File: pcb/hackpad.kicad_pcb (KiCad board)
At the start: 2 copper layers, 21.5 x 50 mm, 4 parts, among them SW1 SW_Push, SW2 SW_Push, SW3 SW_Push, U1 MOUDLE-SEEEDUINO-XIAO

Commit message: Update the schematic
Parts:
- added D1: 1N4148, Diode_THT:D_DO-35_SOD27_P7.62mm_Horizontal, F.Cu at (49.0, 84.6)
- added D10: 1N4148, Diode_THT:D_DO-35_SOD27_P7.62mm_Horizontal, F.Cu at (68.0, 122.7)
- added D11: 1N4148, Diode_THT:D_DO-35_SOD27_P7.62mm_Horizontal, F.Cu at (87.1, 122.7)
- added D12: 1N4148, Diode_THT:D_DO-35_SOD27_P7.62mm_Horizontal, F.Cu at (106.2, 122.7)
- added D2: 1N4148, Diode_THT:D_DO-35_SOD27_P7.62mm_Horizontal, F.Cu at (68.0, 84.6)
- added D3: 1N4148, Diode_THT:D_DO-35_SOD27_P7.62mm_Horizontal, F.Cu at (87.1, 84.6)
- added D4: 1N4148, Diode_THT:D_DO-35_SOD27_P7.62mm_Horizontal, F.Cu at (106.2, 84.6)
- added D5: 1N4148, Diode_THT:D_DO-35_SOD27_P7.62mm_Horizontal, F.Cu at (49.0, 103.7)
- added D6: 1N4148, Diode_THT:D_DO-35_SOD27_P7.62mm_Horizontal, F.Cu at (68.0, 103.7)
- added D7: 1N4148, Diode_THT:D_DO-35_SOD27_P7.62mm_Horizontal, F.Cu at (87.1, 103.7)
- added D8: 1N4148, Diode_THT:D_DO-35_SOD27_P7.62mm_Horizontal, F.Cu at (106.2, 103.7)
- added D9: 1N4148, Diode_THT:D_DO-35_SOD27_P7.62mm_Horizontal, F.Cu at (49.0, 122.7)
- added SW10: SW_Push, Button_Switch_Keyboard:SW_Cherry_MX_1.00u_PCB, F.Cu at (79.0, 108.1)
- added SW11: SW_Push, Button_Switch_Keyboard:SW_Cherry_MX_1.00u_PCB, F.Cu at (98.1, 108.1)
- added SW12: SW_Push, Button_Switch_Keyboard:SW_Cherry_MX_1.00u_PCB, F.Cu at (117.2, 108.1)
- added SW13: RotaryEncoder_Switch, Rotary_Encoder:RotaryEncoder_Alps_EC11E-Switch_Vertical_H20mm, F.Cu at (50.2, 47.5)
- added SW4: SW_Push, Button_Switch_Keyboard:SW_Cherry_MX_1.00u_PCB, F.Cu at (117.2, 70.0)
- added SW5: SW_Push, Button_Switch_Keyboard:SW_Cherry_MX_1.00u_PCB, F.Cu at (60.0, 89.0)
- added SW6: SW_Push, Button_Switch_Keyboard:SW_Cherry_MX_1.00u_PCB, F.Cu at (79.0, 89.0)
- added SW7: SW_Push, Button_Switch_Keyboard:SW_Cherry_MX_1.00u_PCB, F.Cu at (98.1, 89.0)
- added SW8: SW_Push, Button_Switch_Keyboard:SW_Cherry_MX_1.00u_PCB, F.Cu at (117.2, 89.0)
- added SW9: SW_Push, Button_Switch_Keyboard:SW_Cherry_MX_1.00u_PCB, F.Cu at (60.0, 108.1)
- added U2: ER_OLEDM0.91_1x-I2C, Display:ER_OLEDM0.91_1x-I2C, F.Cu at (121.0, 46.7)
- moved SW1 39.2 mm to (60.0, 70.0)
- moved SW2 14.9 mm to (79.0, 70.0)
- moved U1 14.0 mm to (75.1, 52.4)
- moved SW3 9.43 mm to (98.1, 70.0)
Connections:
- SW1 pad 1: Net-(U1-PA6_A10_D10_MOSI) -> /Column 0
- SW1 pad 2: GND -> Net-(D1-A)
- SW2 pad 1: Net-(U1-PA5_A9_D9_MISO) -> /Column 1
- SW2 pad 2: GND -> Net-(D2-A)
- SW3 pad 1: Net-(U1-PA7_A8_D8_SCK) -> /Column 2
- SW3 pad 2: GND -> Net-(D3-A)
- U1 pad 1: unconnected-(U1-PA02_A0_D0-Pad1) -> /Column 0
- U1 pad 12: unconnected-(U1-3V3-Pad12) -> Net-(U1-3V3)
- U1 pad 2: unconnected-(U1-PA4_A1_D1-Pad2) -> /Column 1
- U1 pad 3: unconnected-(U1-PA10_A2_D2-Pad3) -> /Column 2
- U1 pad 4: unconnected-(U1-PA11_A3_D3-Pad4) -> /Column 3
- U1 pad 5: unconnected-(U1-PA8_A4_D4_SDA-Pad5) -> OLED SDA
- U1 pad 6: unconnected-(U1-PA9_A5_D5_SCL-Pad6) -> OLED SCL
- U1 pad 7: unconnected-(U1-PB08_A6_D6_TX-Pad7) -> Net-(D1-K)
- U1 pad 8: unconnected-(U1-PB09_A7_D7_RX-Pad8) -> /Row 1
- U1 pad 9: Net-(U1-PA7_A8_D8_SCK) -> /Row 2
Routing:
- net GND: track 30.2 -> 0.00 mm
- net Net-(U1-PA7_A8_D8_SCK): track 26.2 -> 0.00 mm
- net Net-(U1-PA6_A10_D10_MOSI): track 17.2 -> 0.00 mm
- net Net-(U1-PA5_A9_D9_MISO): track 14.7 -> 0.00 mm
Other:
- board size 21.5 x 50 mm -> 100 x 100 mm

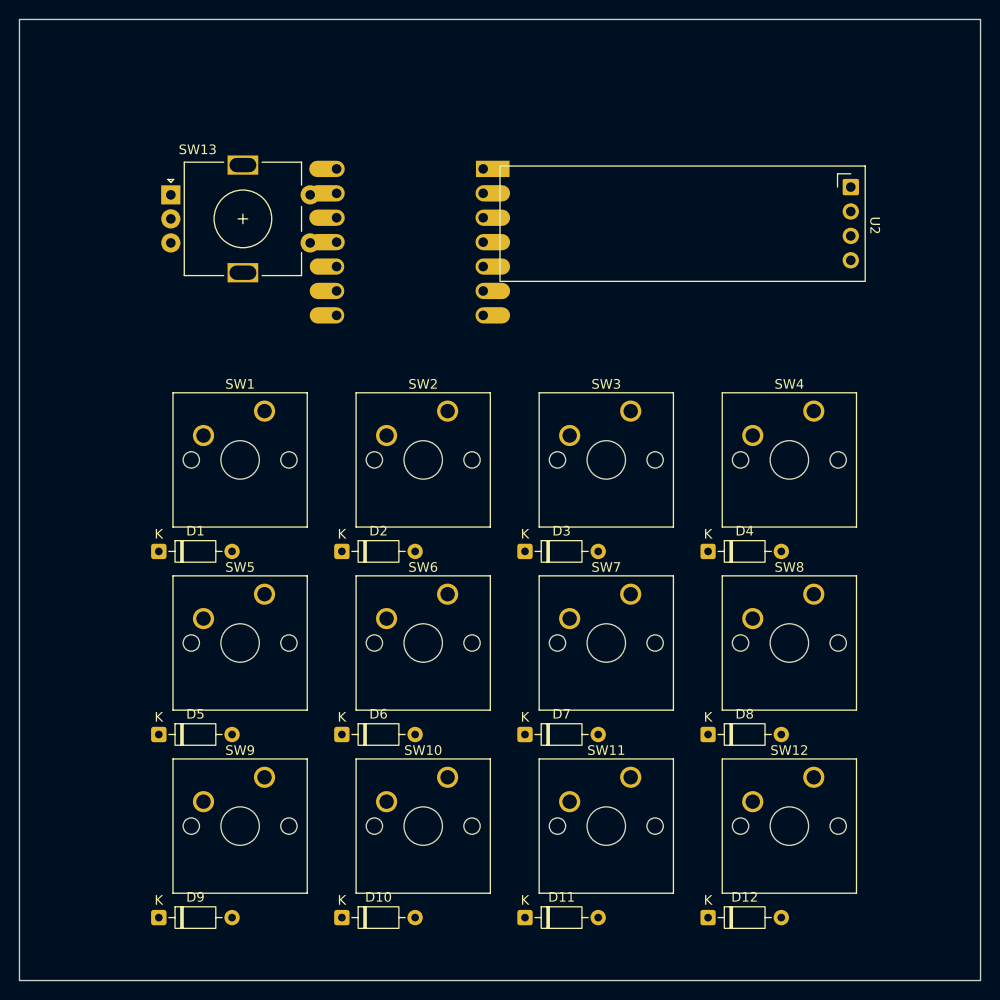
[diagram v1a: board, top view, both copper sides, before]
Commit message: Re-route PCB and update the case
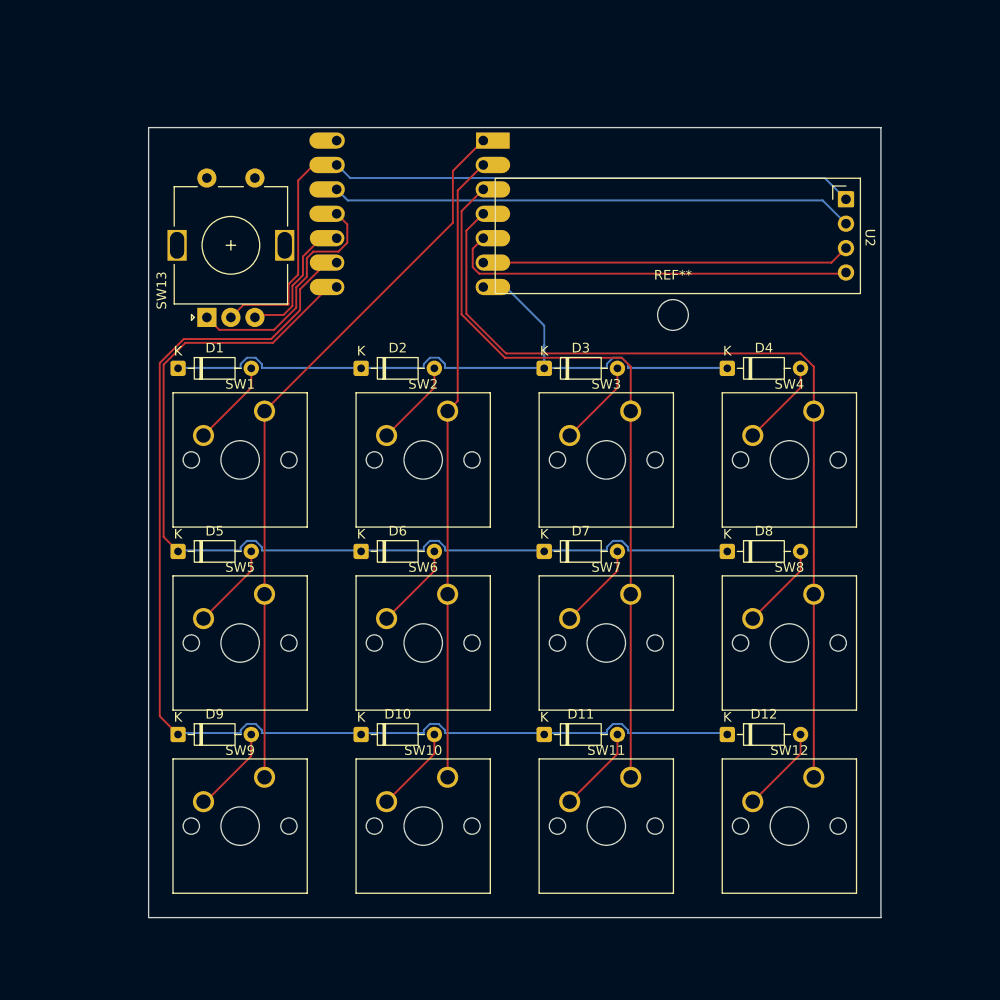
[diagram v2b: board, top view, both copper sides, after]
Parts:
- added REF**: MountingHole_3.2mm_M3, MountingHole:MountingHole_3.2mm_M3, F.Cu at (102.5, 60.0)
- moved D5 19.2 mm to (51.0, 84.6)
- moved D6 19.2 mm to (70.0, 84.6)
- moved D7 19.2 mm to (89.1, 84.6)
- moved D8 19.2 mm to (108.2, 84.6)
- moved D1 19.2 mm to (51.0, 65.5)
- moved D10 19.2 mm to (70.0, 103.7)
- moved D11 19.2 mm to (89.1, 103.7)
- moved D12 19.2 mm to (108.2, 103.7)
- moved D2 19.2 mm to (70.0, 65.5)
- moved D3 19.2 mm to (89.1, 65.5)
- moved D4 19.2 mm to (108.2, 65.5)
- moved D9 19.2 mm to (51.0, 103.7)
- moved SW13 13.3 mm to (54.0, 60.2), turned to 90 degrees
- moved U1 2.95 mm to (75.1, 49.5)
- moved U2 1.36 mm to (120.5, 48.0)
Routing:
- net /Row 2: track 0.00 -> 125.4 mm
- net /Row 1: track 0.00 -> 103.3 mm
- net /Column 3: track 0.00 -> 92.3 mm
- net GND: track 0.00 -> 81.5 mm
- net Net-(D1-K): track 0.00 -> 78.5 mm
- net /Column 2: track 0.00 -> 76.5 mm
- net /Column 0: track 0.00 -> 75.7 mm
- net /Column 1: track 0.00 -> 65.2 mm
- net Net-(U1-3V3): track 0.00 -> 54.5 mm
- net OLED SDA: track 0.00 -> 42.6 mm
- net OLED SCL: track 0.00 -> 38.4 mm
- net Net-(U1-PA6_A10_D10_MOSI): track 0.00 -> 24.7 mm
- net Net-(U1-PA5_A9_D9_MISO): track 0.00 -> 16.3 mm
- net Net-(D9-A): track 0.00 -> 9.20 mm
- net Net-(D5-A): track 0.00 -> 9.07 mm
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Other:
- board size 100 x 100 mm -> 76.2 x 82.2 mm

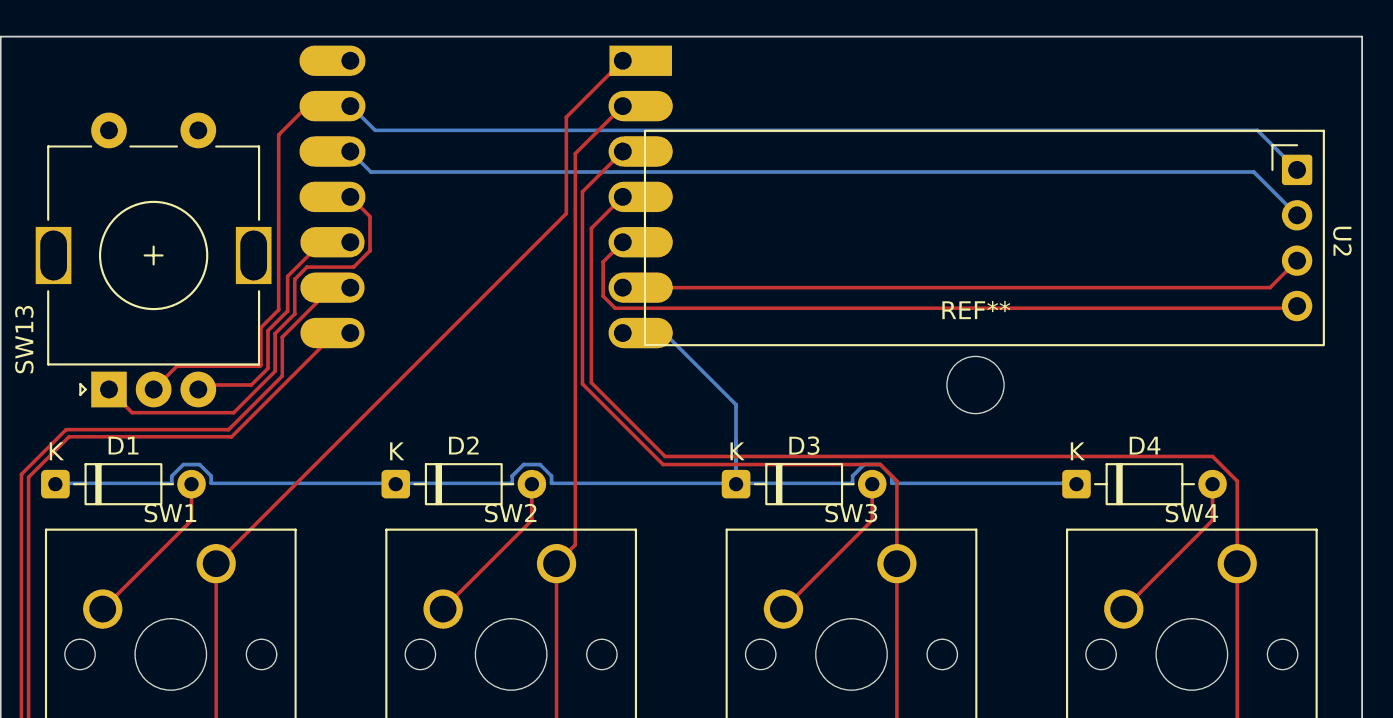
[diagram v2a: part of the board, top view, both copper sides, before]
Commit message: Fix pcb error and reorganize folders
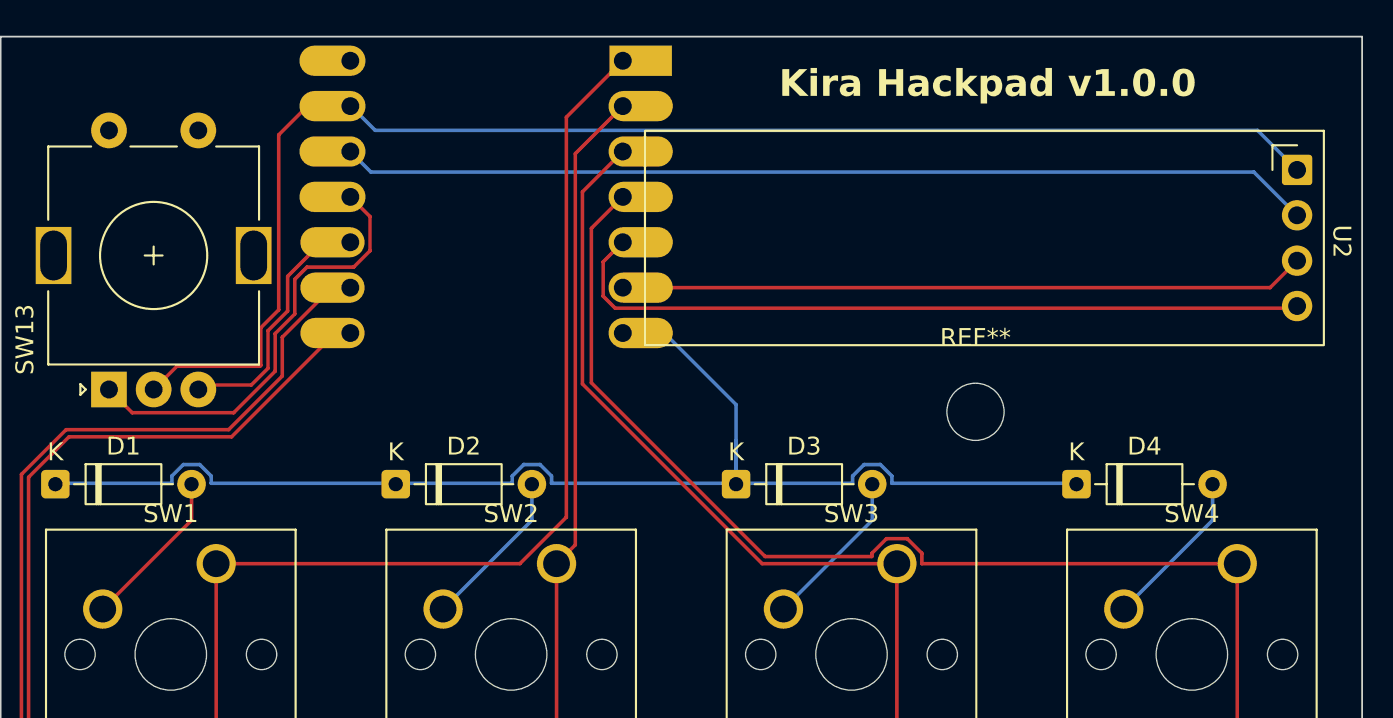
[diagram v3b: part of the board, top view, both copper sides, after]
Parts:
- moved REF** 1.50 mm to (102.5, 61.5)
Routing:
- net /Column 0: track 75.7 -> 85.7 mm
- net /Column 2: track 76.5 -> 73.8 mm
- net /Column 3: track 92.3 -> 90.8 mm
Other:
- board text added: "Kira Hackpad v1.0.0"
